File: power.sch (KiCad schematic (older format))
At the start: 4 parts, among them J201 Power_Planes, Q201 Q_PMOS_GSD

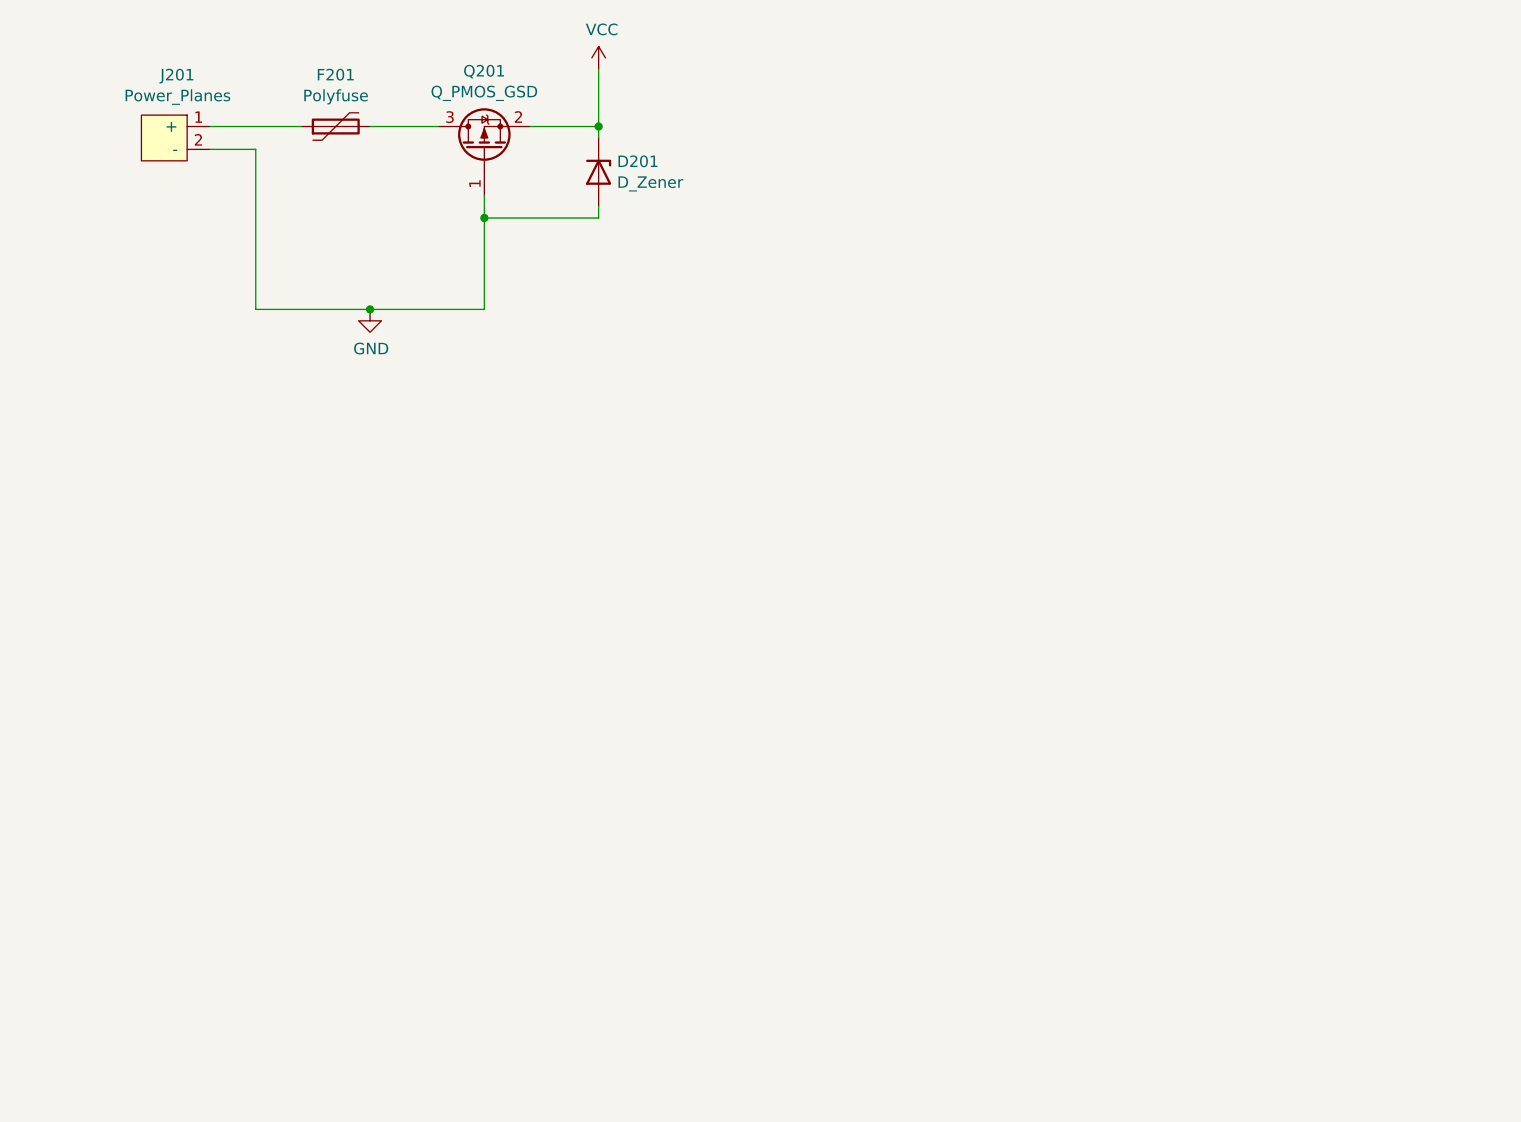
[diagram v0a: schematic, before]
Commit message: Added a LDO, maybe not the final one but there is one on the PCB now. Added a voltage divider for measureing battery voltage.
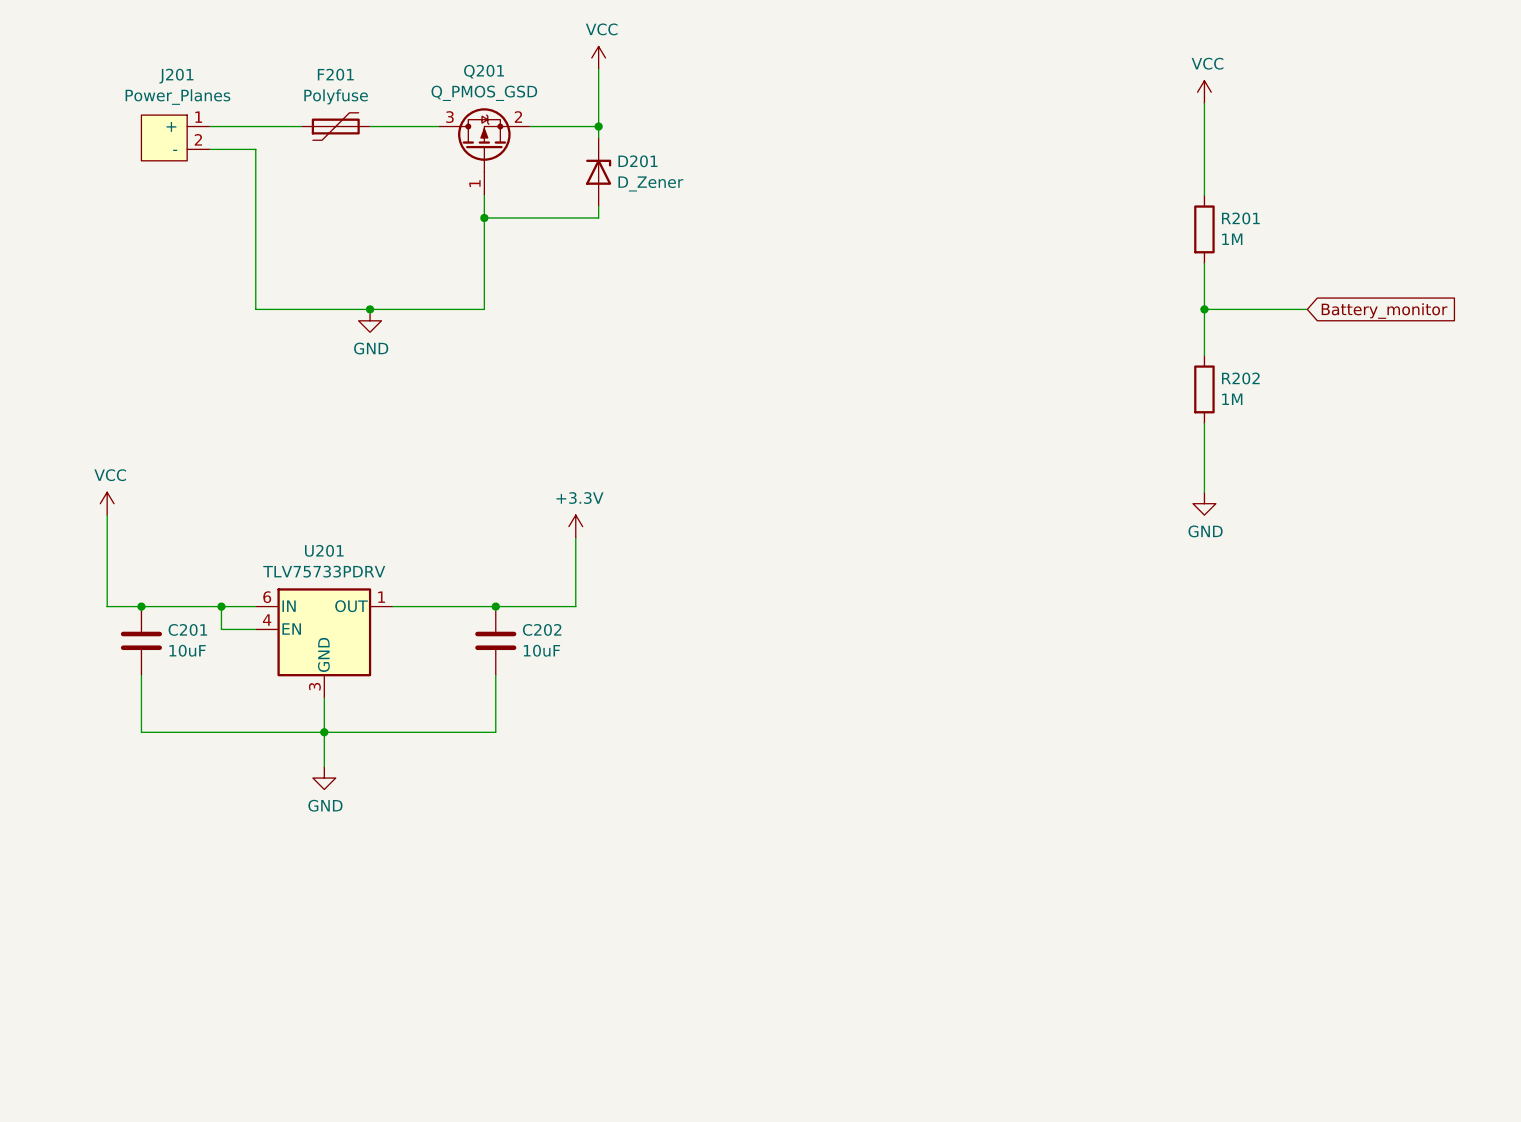
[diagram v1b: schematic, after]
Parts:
- added C201, C202: 10uF, symbol Device:C
- added R201, R202: 1M, Resistor_SMD:R_0603_1608Metric_Pad0.98x0.95mm_HandSolder, symbol Device:R
- added U201: TLV75733PDRV, Package_SON:WSON-6-1EP_2x2mm_P0.65mm_EP1x1.6mm, symbol Regulator_Linear:TLV75733PDRV
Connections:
- net GND: now also C201.1, C202.2, R202.2, U201.3 (GND), U201.7 (GND)
- net VCC: now also C201.2, R201.1, U201.4 (EN), U201.6 (IN)
- new net +3V3: C202.1, U201.1 (OUT)
- new net Battery_monitor: R201.2, R202.1
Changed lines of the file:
@@
 	3250 1600 3250 2000
 Connection ~ 2750 2000
+$Comp
+L Regulator_Linear:TLV75733PDRV U201
+U 1 1 61410663
+P 2550 3400
+F 0 "U201" H 2550 3742 50  0000 C CNN
+F 1 "TLV75733PDRV" H 2550 3651 50  0000 C CNN
+F 2 "Package_SON:WSON-6-1EP_2x2mm_P0.65mm_EP1x1.6mm" H 2550 3725 50  0001 C CIN
+F 3 "https://www.ti.com/lit/ds/symlink/tlv757p.pdf" H 2550 3450 50  0001 C CNN
+	1    2550 3400
+	1    0    0    -1
+$EndComp
+$Comp
+L power:+3.3V #PWR0118
+U 1 1 61417284
+P 3650 3000
+F 0 "#PWR0118" H 3650 2850 50  0001 C CNN
+F 1 "+3.3V" H 3665 3173 50  0000 C CNN
+F 2 "" H 3650 3000 50  0001 C CNN
+F 3 "" H 3650 3000 50  0001 C CNN
+	1    3650 3000
+	1    0    0    -1
+$EndComp
+$Comp
+L power:VCC #PWR0119
+U 1 1 6141906A
+P 1600 2900
+F 0 "#PWR0119" H 1600 2750 50  0001 C CNN
+F 1 "VCC" H 1615 3073 50  0000 C CNN
+F 2 "" H 1600 2900 50  0001 C CNN
+F 3 "" H 1600 2900 50  0001 C CNN
+	1    1600 2900
+	1    0    0    -1
+$EndComp
+$Comp
+L power:GND #PWR0120
+U 1 1 6141A610
+P 2550 4000
+F 0 "#PWR0120" H 2550 3750 50  0001 C CNN
+F 1 "GND" H 2555 3827 50  0000 C CNN
+F 2 "" H 2550 4000 50  0001 C CNN
+F 3 "" H 2550 4000 50  0001 C CNN
+	1    2550 4000
+	1    0    0    -1
+$EndComp
+Wire Wire Line
+	2850 3300 3300 3300
+Wire Wire Line
+	3650 3300 3650 3000
+Wire Wire Line
+	1600 2900 1600 3300
+Wire Wire Line
+	2250 3400 2100 3400
+Wire Wire Line
+	2100 3400 2100 3300
+Connection ~ 2100 3300
+Wire Wire Line
+	2100 3300 2250 3300
+Wire Wire Line
+	2550 3700 2550 3850
+$Comp
+L Device:R R201
+U 1 1 6141B73C
+P 6400 1650
+F 0 "R201" H 6470 1696 50  0000 L CNN
+F 1 "1M" H 6470 1605 50  0000 L CNN
+F 2 "Resistor_SMD:R_0603_1608Metric_Pad0.98x0.95mm_HandSolder" V 6330 1650 50  0001 C CNN
+F 3 "~" H 6400 1650 50  0001 C CNN
+	1    6400 1650
+	1    0    0    -1
+$EndComp
+$Comp
+L Device:R R202
+U 1 1 6141DF1C
+P 6400 2350
+F 0 "R202" H 6470 2396 50  0000 L CNN
+F 1 "1M" H 6470 2305 50  0000 L CNN
+F 2 "Resistor_SMD:R_0603_1608Metric_Pad0.98x0.95mm_HandSolder" V 6330 2350 50  0001 C CNN
+F 3 "~" H 6400 2350 50  0001 C CNN
+	1    6400 2350
+	1    0    0    -1
+$EndComp
+$Comp
+L power:VCC #PWR0121
+U 1 1 61420C16
+P 6400 1100
+F 0 "#PWR0121" H 6400 950 50  0001 C CNN
+F 1 "VCC" H 6415 1273 50  0000 C CNN
+F 2 "" H 6400 1100 50  0001 C CNN
+F 3 "" H 6400 1100 50  0001 C CNN
+	1    6400 1100
+	1    0    0    -1
+$EndComp
+Wire Wire Line
+	6400 1100 6400 1500
+Wire Wire Line
+	6400 1800 6400 2000
+$Comp
+L power:GND #PWR0122
+U 1 1 614222F9
+P 6400 2800
+F 0 "#PWR0122" H 6400 2550 50  0001 C CNN
+F 1 "GND" H 6405 2627 50  0000 C CNN
+F 2 "" H 6400 2800 50  0001 C CNN
+F 3 "" H 6400 2800 50  0001 C CNN
+	1    6400 2800
+	1    0    0    -1
+$EndComp
+Wire Wire Line
+	6400 2500 6400 2800
+Text GLabel 6850 2000 2    50   Input ~ 0
+Battery_monitor
+Wire Wire Line
+	6850 2000 6400 2000
+Connection ~ 6400 2000
+Wire Wire Line
+	6400 2000 6400 2200
+$Comp
+L Device:C C202
+U 1 1 61422CB1
+P 3300 3450
+F 0 "C202" H 3415 3496 50  0000 L CNN
+F 1 "10uF" H 3415 3405 50  0000 L CNN
+F 2 "" H 3338 3300 50  0001 C CNN
+F 3 "~" H 3300 3450 50  0001 C CNN
+	1    3300 3450
+	1    0    0    -1
+$EndComp
+Connection ~ 3300 3300
+Wire Wire Line
+	3300 3300 3650 3300
+$Comp
+L Device:C C201
+U 1 1 61423AB5
+P 1750 3450
+F 0 "C201" H 1635 3404 50  0000 R CNN
+F 1 "10uF" H 1635 3495 50  0000 R CNN
+F 2 "" H 1788 3300 50  0001 C CNN
+F 3 "~" H 1750 3450 50  0001 C CNN
+	1    1750 3450
+	-1   0    0    1
+$EndComp
+Wire Wire Line
+	3300 3600 3300 3850
+Wire Wire Line
+	3300 3850 2550 3850
+Connection ~ 2550 3850
+Wire Wire Line
+	2550 3850 2550 4000
+Wire Wire Line
+	2550 3850 1750 3850
+Wire Wire Line
+	1750 3850 1750 3600
+Wire Wire Line
+	1600 3300 1750 3300
+Connection ~ 1750 3300
+Wire Wire Line
+	1750 3300 2100 3300
 $EndSCHEMATC

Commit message: Added some 1206 caps to be large stabilizing capacitors. Added a rank 1 RC filter to audio out, with a bypass solderbridge if wanted.
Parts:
- C201, C202: footprint (none) -> Capacitor_SMD:C_1206_3216Metric
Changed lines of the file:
@@
 F 0 "C202" H 3415 3496 50  0000 L CNN
 F 1 "10uF" H 3415 3405 50  0000 L CNN
-F 2 "" H 3338 3300 50  0001 C CNN
+F 2 "Capacitor_SMD:C_1206_3216Metric" H 3338 3300 50  0001 C CNN
 F 3 "~" H 3300 3450 50  0001 C CNN
 	1    3300 3450
@@
 F 0 "C201" H 1635 3404 50  0000 R CNN
 F 1 "10uF" H 1635 3495 50  0000 R CNN
-F 2 "" H 1788 3300 50  0001 C CNN
+F 2 "Capacitor_SMD:C_1206_3216Metric" H 1788 3300 50  0001 C CNN
 F 3 "~" H 1750 3450 50  0001 C CNN
 	1    1750 3450

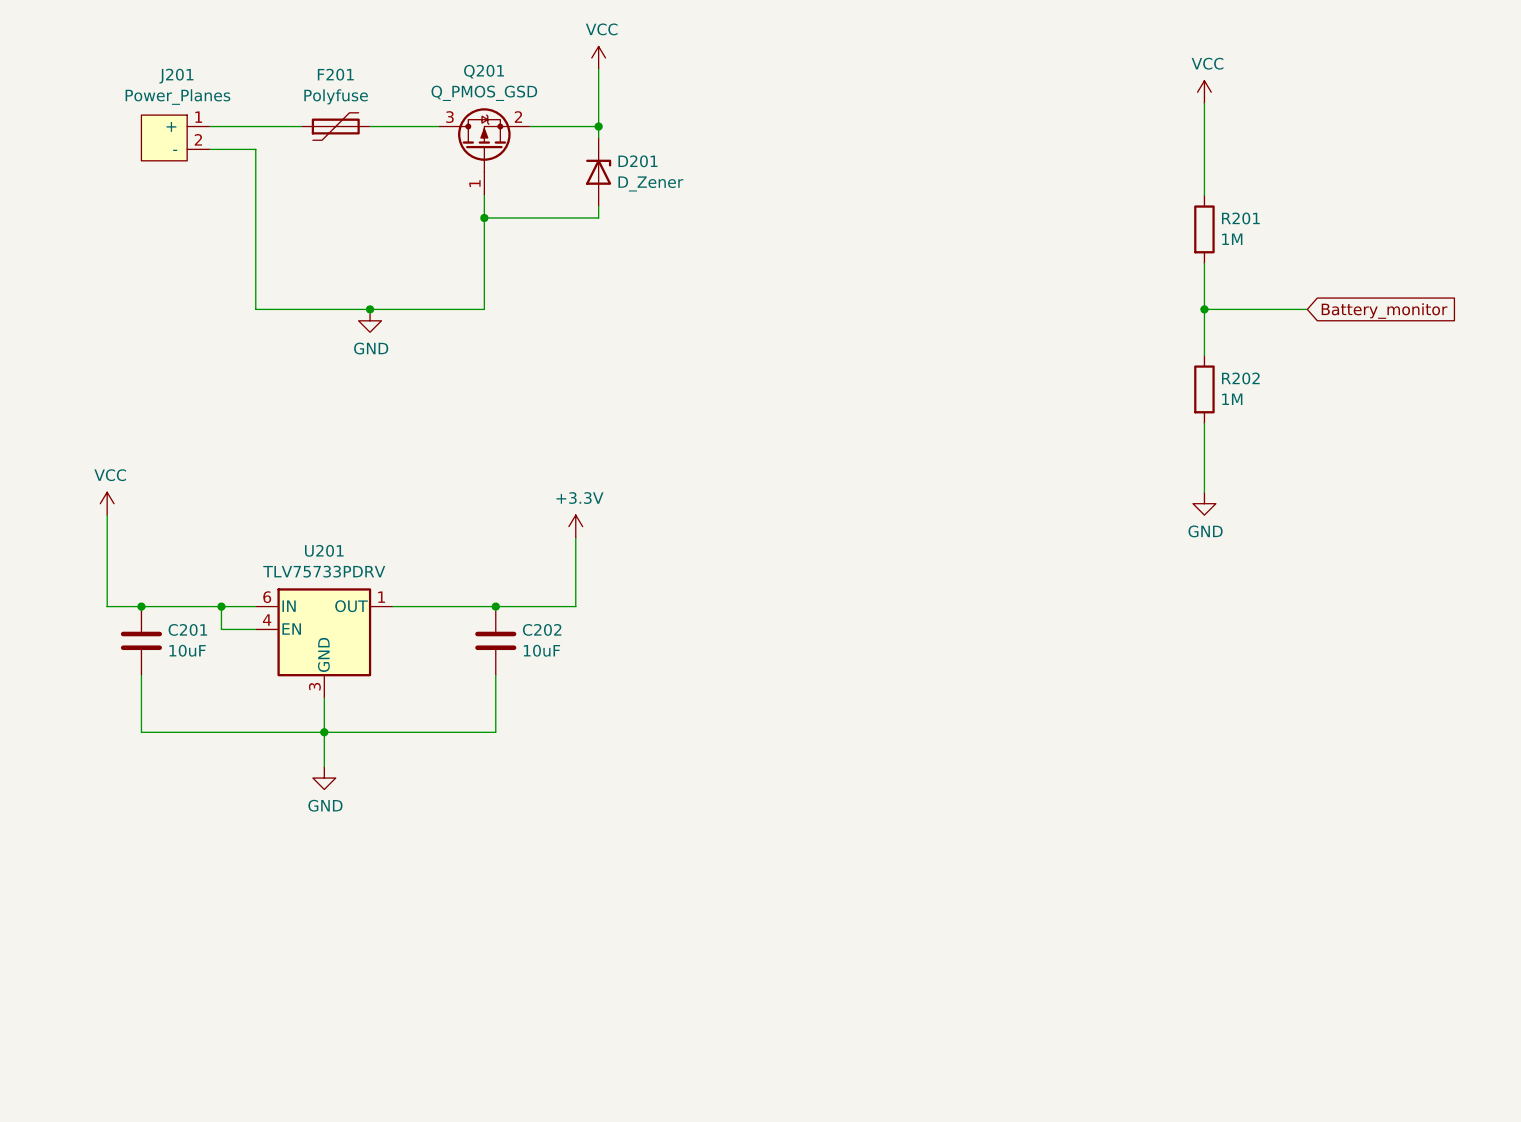
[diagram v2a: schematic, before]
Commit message: Added some primitive filter for 3V3A and GNDA. Added the IMU to the board.
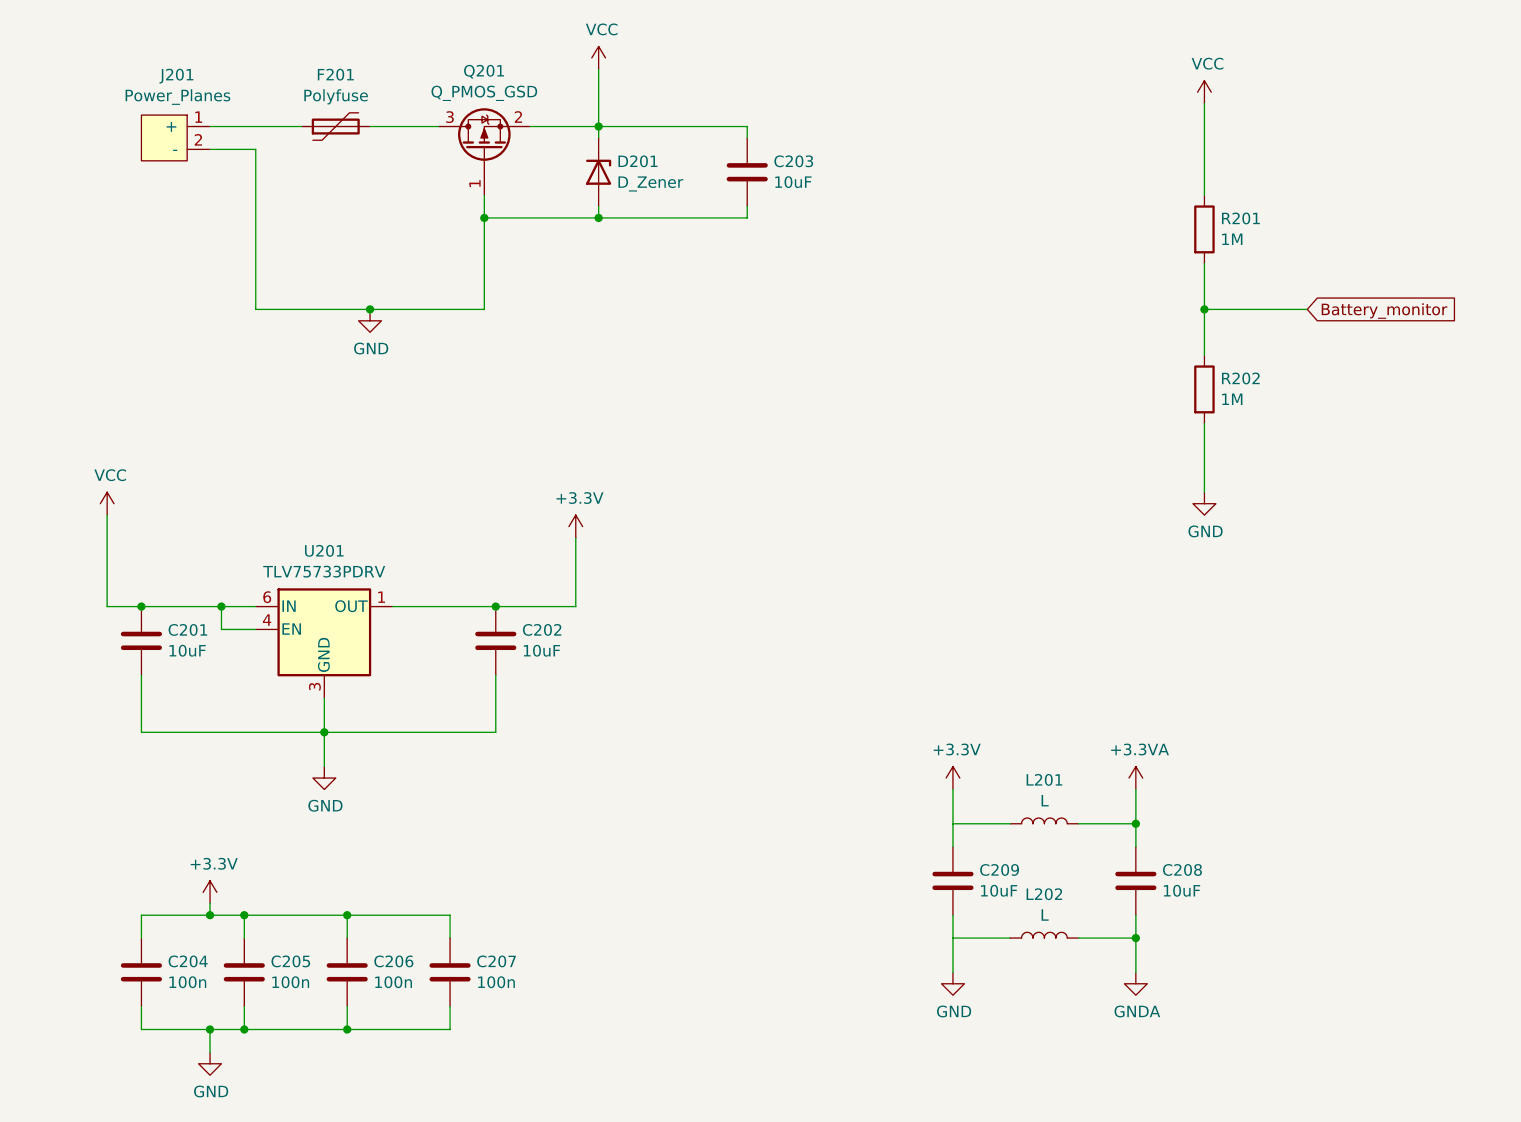
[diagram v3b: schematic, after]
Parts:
- added C203, C208, C209: 10uF, Capacitor_SMD:C_1206_3216Metric, symbol Device:C
- added C204, C205, C206, C207: 100n, Capacitor_SMD:C_0603_1608Metric_Pad1.08x0.95mm_HandSolder, symbol Device:C
- added L201, L202: L, Inductor_SMD:L_1206_3216Metric_Pad1.42x1.75mm_HandSolder, symbol Device:L
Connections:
- net +3V3: now also C204.1, C205.1, C206.1, C207.1, C209.1, L201.1
- net GND: now also C203.2, C204.2, C205.2, C206.2, C207.2, C209.2, L202.1
- net VCC: now also C203.1
- new net +3.3VA: C208.1, L201.2
- new net GNDA: C208.2, L202.2
